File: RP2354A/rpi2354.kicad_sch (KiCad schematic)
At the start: 37 parts, among them J201 TC2030-NL, SW201 SW_Push_DPDT, U201 RP2354A, U202 NCP1117-3.3_SOT223, Y201 ABM8-272-T3

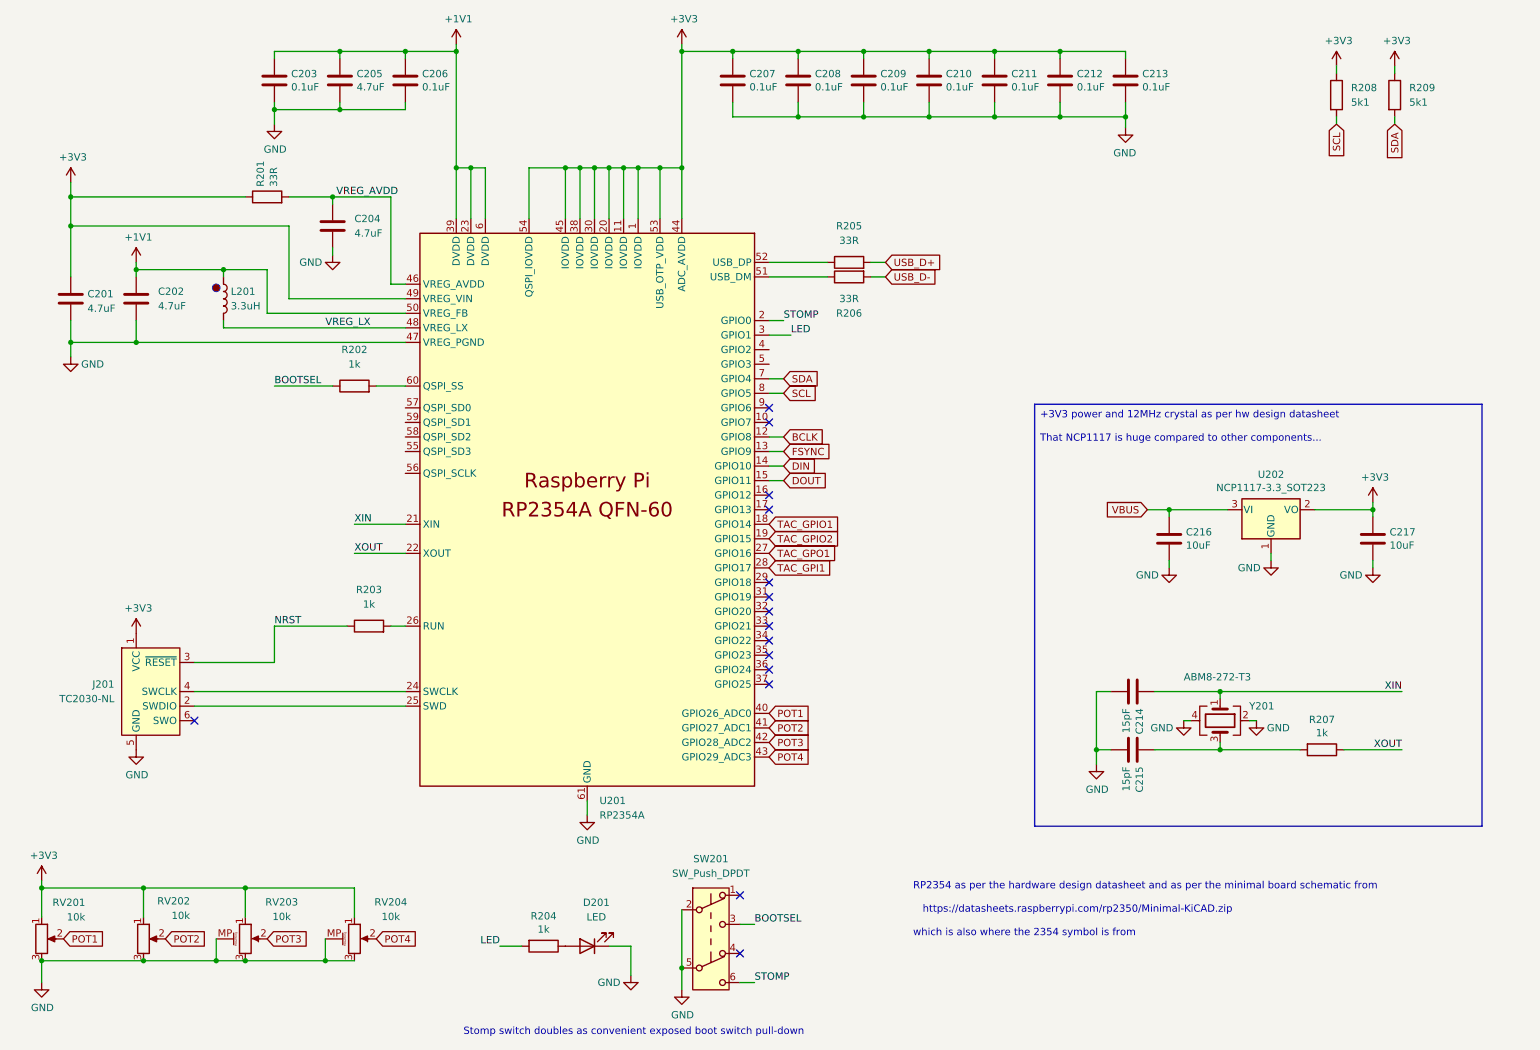
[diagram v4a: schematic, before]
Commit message: rp2354: First stab at pcb layout
This is an insane 6-layer stackup, not because I need six layers
(although it does allow me to be even lazier than usual), but because I
want to use via-in-pad and at that point jlcpcb pretty much ends up
doing the whole precision 6-layer thing anyway.

The minimal RP2354A board makes do with just a simple two-layer stackup,
and I'm sure this could have been done that way too.  But with four
layers it's easy to just use one layer for the +1V1 zone and one for the
+3V3 zone under the RP2354A, and just bring things in with the vias.

This is all connected, but with some ERC noise. Mostly harmless (tm).

Also add JLCPCB part numbers to things, although I need to check them
all several times.

Signed-off-by: Linus Torvalds <torvalds@linux-foundation.org>
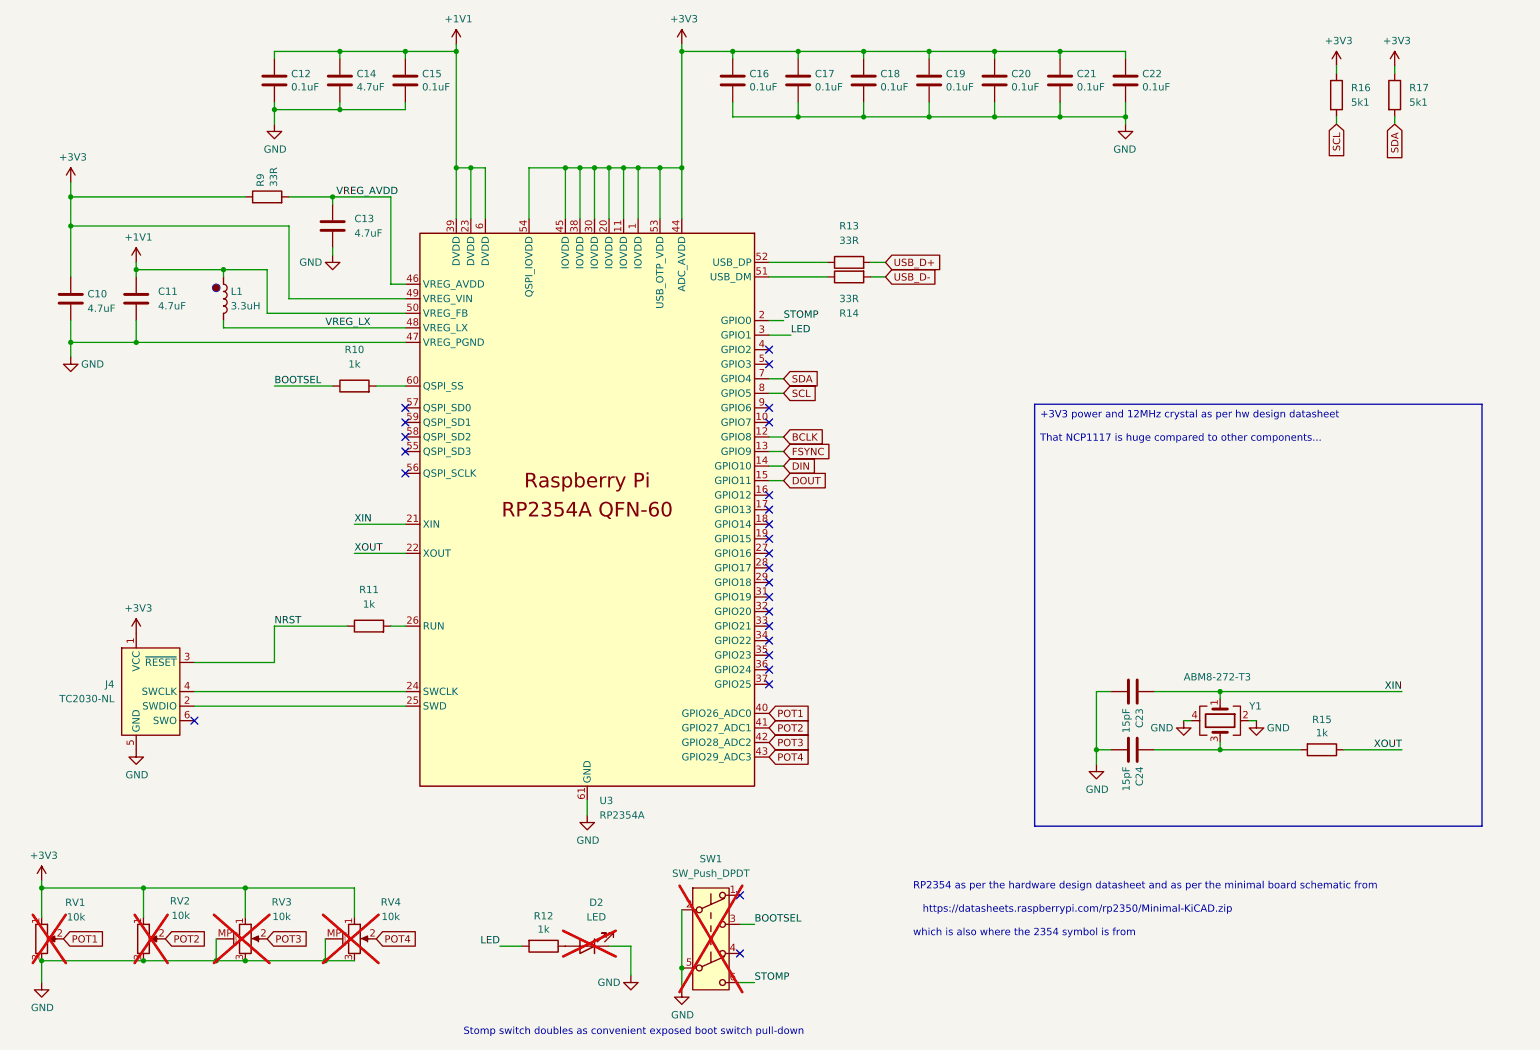
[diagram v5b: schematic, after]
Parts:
- removed C216, C217: 10uF, Capacitor_SMD:C_0603_1608Metric, symbol Device:C
- removed U202: NCP1117-3.3_SOT223, Package_TO_SOT_SMD:SOT-223-3_TabPin2, symbol Regulator_Linear:NCP1117-3.3_SOT223
- C10: renamed from C201; JLCPCB (none) -> C22399629
- C11: renamed from C202; JLCPCB (none) -> C22399629
- C12: renamed from C203; JLCPCB (none) -> C1525
- C13: renamed from C204; JLCPCB (none) -> C22399629
- C14: renamed from C205; JLCPCB (none) -> C22399629
- C15: renamed from C206; JLCPCB (none) -> C1525
- C16: renamed from C207; JLCPCB (none) -> C1525
- C17: renamed from C208; JLCPCB (none) -> C1525
- C18: renamed from C209; JLCPCB (none) -> C1525
- C19: renamed from C210; JLCPCB (none) -> C1525
- C20: renamed from C211; JLCPCB (none) -> C1525
- C21: renamed from C212; JLCPCB (none) -> C1525
- C22: renamed from C213; JLCPCB (none) -> C1525
- C23: renamed from C214; JLCPCB (none) -> C1548
- C24: renamed from C215; JLCPCB (none) -> C1548
- D2: renamed from D201; now not fitted
- L1: renamed from L201; JLCPCB (none) -> C42411119
- R10: renamed from R202; JLCPCB (none) -> C11702
- R11: renamed from R203; JLCPCB (none) -> C11702
- R12: renamed from R204; JLCPCB (none) -> C11702
- R13: renamed from R205; JLCPCB (none) -> C25105
- R14: renamed from R206; JLCPCB (none) -> C25105
- R15: renamed from R207; JLCPCB (none) -> C11702
- R16: renamed from R208; JLCPCB (none) -> C25905
- R17: renamed from R209; JLCPCB (none) -> C25905
- R9: renamed from R201; JLCPCB (none) -> C25105
- RV1: renamed from RV201; now not fitted
- RV2: renamed from RV202; now not fitted
- RV3: renamed from RV203; now not fitted
- RV4: renamed from RV204; now not fitted
- SW1: renamed from SW201; now not fitted
- U3: renamed from U201; JLCPCB (none) -> C41378174
- Y1: renamed from Y201; JLCPCB (none) -> C20625731
- renumbered J201 to J4
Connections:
- net TAC_GPI1: no longer names the net of U3.28 (GPIO17)
- net TAC_GPIO1: no longer names the net of U3.18 (GPIO14)
- net TAC_GPIO2: no longer names the net of U3.19 (GPIO15)
- net TAC_GPO1: no longer names the net of U3.27 (GPIO16)
- no-connect marks 15 -> 26

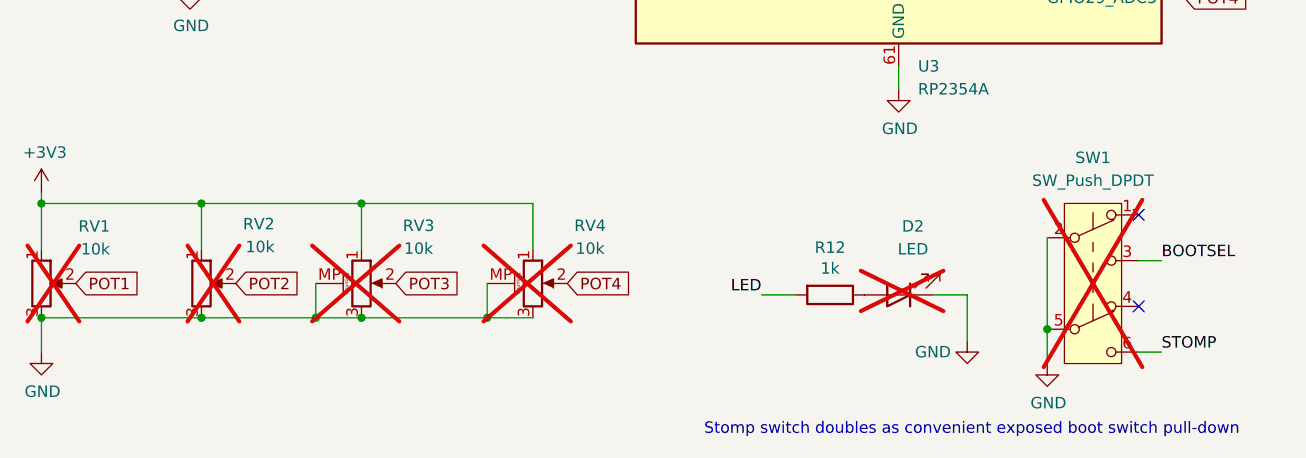
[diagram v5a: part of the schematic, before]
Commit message: Fix missing JLCPCB number, and replace "DNP" with "not in BOM"
Also cross-verify the JLCPCB numbers.

Signed-off-by: Linus Torvalds <torvalds@linux-foundation.org>
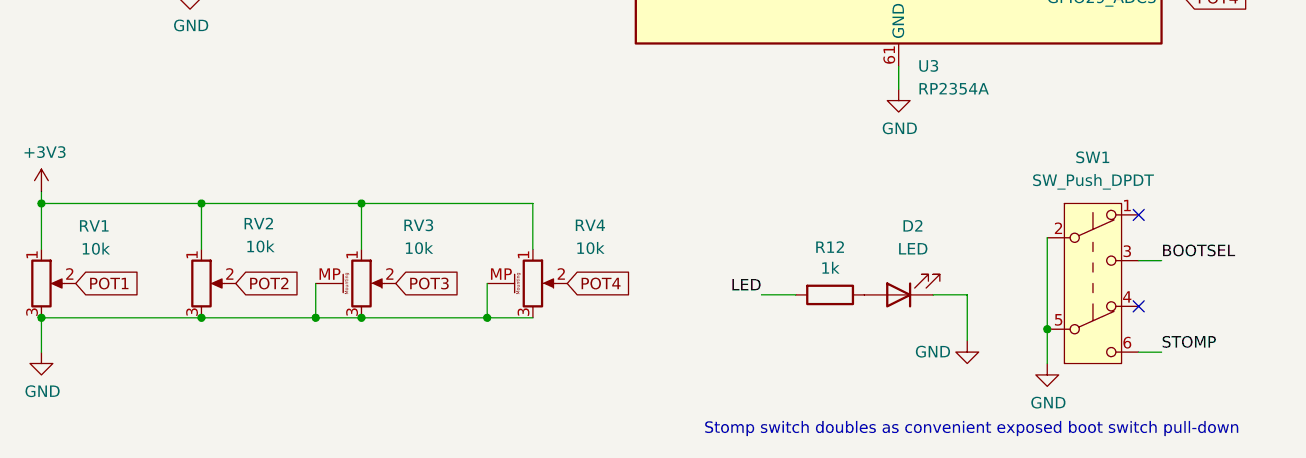
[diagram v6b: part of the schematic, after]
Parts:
- D2, RV1, RV2, RV3, RV4, SW1: now fitted; now left out of the parts list
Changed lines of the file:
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@@
 		(unit 1)
 		(exclude_from_sim no)
-		(in_bom yes)
+		(in_bom no)
 		(on_board yes)
-		(dnp yes)
+		(dnp no)
 		(property "Reference" "RV1"
 			(at 35.56 172.72 0)
@@
 		(unit 1)
 		(exclude_from_sim no)
-		(in_bom yes)
+		(in_bom no)
 		(on_board yes)
-		(dnp yes)
+		(dnp no)
 		(fields_autoplaced yes)
 		(property "Reference" "RV3"
@@
 		(unit 1)
 		(exclude_from_sim no)
-		(in_bom yes)
+		(in_bom no)
 		(on_board yes)
-		(dnp yes)
+		(dnp no)
 		(fields_autoplaced yes)
 		(property "Reference" "RV4"
@@
 		(unit 1)
 		(exclude_from_sim no)
-		(in_bom yes)
+		(in_bom no)
 		(on_board yes)
-		(dnp yes)
+		(dnp no)
 		(property "Reference" "RV2"
 			(at 53.848 172.466 0)
@@
 		(unit 1)
 		(exclude_from_sim yes)
-		(in_bom yes)
+		(in_bom no)
 		(on_board yes)
-		(dnp yes)
+		(dnp no)
 		(fields_autoplaced yes)
 		(property "Reference" "SW1"
@@
 		(unit 1)
 		(exclude_from_sim no)
-		(in_bom yes)
+		(in_bom no)
 		(on_board yes)
-		(dnp yes)
+		(dnp no)
 		(fields_autoplaced yes)
 		(property "Reference" "D2"

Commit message: Rename the "JLCPCB" property as "LCSC PN"
That's apparently the standard way for the 'JLCPCB Fabrication Toolkit'
scripting.  At least for the first time, I want to cross-check with the
scripting, even if I might not necessarily use it as-is.

Signed-off-by: Linus Torvalds <torvalds@linux-foundation.org>
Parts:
- C10, C11, C13, C14: JLCPCB C22399629 -> (none); LCSC PN (none) -> C22399629
- C12, C15, C16, C17, C18, C19, C20, C21, C22: JLCPCB C1525 -> (none); LCSC PN (none) -> C1525
- C23, C24: JLCPCB C1548 -> (none); LCSC PN (none) -> C1548
- L1: JLCPCB C42411119 -> (none); LCSC PN (none) -> C42411119
- R10, R11, R12, R15: JLCPCB C11702 -> (none); LCSC PN (none) -> C11702
- R13, R14, R9: JLCPCB C25105 -> (none); LCSC PN (none) -> C25105
- R16, R17: JLCPCB C25905 -> (none); LCSC PN (none) -> C25905
- U3: JLCPCB C41378174 -> (none); LCSC PN (none) -> C41378174
- Y1: JLCPCB C20625731 -> (none); LCSC PN (none) -> C20625731
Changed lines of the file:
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@@
 			)
 		)
-		(property "JLCPCB" "C1525"
+		(property "LCSC PN" "C1525"
 			(at 148.59 29.21 0)
 			(effects
@@
 			)
 		)
-		(property "JLCPCB" "C1525"
+		(property "LCSC PN" "C1525"
 			(at 160.02 29.21 0)
 			(effects
@@
 			)
 		)
-		(property "JLCPCB" "C1525"
+		(property "LCSC PN" "C1525"
 			(at 171.45 29.21 0)
 			(effects
@@
 			)
 		)
-		(property "JLCPCB" "C1525"
+		(property "LCSC PN" "C1525"
 			(at 182.88 29.21 0)
 			(effects
@@
 			)
 		)
-		(property "JLCPCB" "C1525"
+		(property "LCSC PN" "C1525"
 			(at 194.31 29.21 0)
 			(effects
@@
 			)
 		)
-		(property "JLCPCB" "C1525"
+		(property "LCSC PN" "C1525"
 			(at 205.74 29.21 0)
 			(effects
@@
 			)
 		)
-		(property "JLCPCB" ""
+		(property "LCSC PN" ""
 			(at 27.94 179.07 0)
 			(effects
@@
 			)
 		)
-		(property "JLCPCB" "C1525"
+		(property "LCSC PN" "C1525"
 			(at 91.44 29.21 0)
 			(effects
@@
 			)
 		)
-		(property "JLCPCB" "C25905"
+		(property "LCSC PN" "C25905"
 			(at 254 31.75 0)
 			(effects
@@
 			)
 		)
-		(property "JLCPCB" "C11702"
+		(property "LCSC PN" "C11702"
 			(at 82.55 82.55 90)
 			(effects
@@
 			)
 		)
-		(property "JLCPCB" "C1525"
+		(property "LCSC PN" "C1525"
 			(at 217.17 29.21 0)
 			(effects
@@
 			)
 		)
-		(property "JLCPCB" "C11702"
+		(property "LCSC PN" "C11702"
 			(at 115.57 180.34 90)
 			(effects
@@
 			)
 		)
-		(property "JLCPCB" "C25105"
+		(property "LCSC PN" "C25105"
 			(at 168.91 60.96 90)
 			(effects
@@
 			)
 		)
-		(property "JLCPCB" "C25105"
+		(property "LCSC PN" "C25105"
 			(at 67.31 49.53 0)
 			(effects
@@
 			)
 		)
-		(property "JLCPCB" "C22399629"
+		(property "LCSC PN" "C22399629"
 			(at 33.02 67.31 0)
 			(effects
@@
 			)
 		)
-		(property "JLCPCB" "C1548"
+		(property "LCSC PN" "C1548"
 			(at 218.44 146.05 0)
 			(effects
@@
 			)
 		)
-		(property "JLCPCB" "C22399629"
+		(property "LCSC PN" "C22399629"
 			(at 44.45 67.31 0)
 			(effects
@@
 			)
 		)
-		(property "JLCPCB" "C22399629"
+		(property "LCSC PN" "C22399629"
 			(at 78.74 54.61 0)
 			(effects
@@
 			)
 		)
-		(property "JLCPCB" "C41378174"
+		(property "LCSC PN" "C41378174"
 			(at 123.19 87.63 0)
 			(effects
@@
 			)
 		)
-		(property "JLCPCB" ""
+		(property "LCSC PN" ""
 			(at 46.99 135.89 0)
 			(effects
@@
 			)
 		)
-		(property "JLCPCB" "C11702"
+		(property "LCSC PN" "C11702"
 			(at 251.46 146.05 90)
 			(effects
@@
 			)
 		)
-		(property "JLCPCB" "C25105"
+		(property "LCSC PN" "C25105"
 			(at 168.91 63.5 90)
 			(effects
@@
 			)
 		)
-		(property "JLCPCB" "C1525"
+		(property "LCSC PN" "C1525"
 			(at 68.58 29.21 0)
 			(effects
@@
 			)
 		)
-		(property "JLCPCB" "C11702"
+		(property "LCSC PN" "C11702"
 			(at 85.09 124.46 90)
 			(effects
@@
 			)
 		)
-		(property "JLCPCB" ""
+		(property "LCSC PN" ""
 			(at 63.5 179.07 0)
 			(effects
@@
 			)
 		)
-		(property "JLCPCB" "C22399629"
+		(property "LCSC PN" "C22399629"
 			(at 80.01 29.21 0)
 			(effects
@@
 			)
 		)
-		(property "JLCPCB" ""
+		(property "LCSC PN" ""
 			(at 82.55 179.07 0)
 			(effects
@@
 			)
 		)
-		(property "JLCPCB" "C42411119"
+		(property "LCSC PN" "C42411119"
 			(at 59.69 67.31 0)
 			(effects
@@
 			)
 		)
-		(property "JLCPCB" ""
+		(property "LCSC PN" ""
 			(at 45.72 179.07 0)
 			(effects
@@
 			)
 		)
-		(property "JLCPCB" "C20625731"
+		(property "LCSC PN" "C20625731"
 			(at 233.68 140.97 90)
 			(effects
@@
 			)
 		)
-		(property "JLCPCB" ""
+		(property "LCSC PN" ""
 			(at 144.78 179.07 0)
 			(effects
@@
 			)
 		)
-		(property "JLCPCB" ""
+		(property "LCSC PN" ""
 			(at 123.19 180.34 0)
 			(effects
@@
 			)
 		)
-		(property "JLCPCB" "C1548"
+		(property "LCSC PN" "C1548"
 			(at 218.44 135.89 0)
 			(effects
@@
 			)
 		)
-		(property "JLCPCB" "C25905"
+		(property "LCSC PN" "C25905"
 			(at 264.16 31.75 0)
 			(effects
